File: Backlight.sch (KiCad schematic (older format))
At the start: 29 parts, among them Q201 FDN5618P, Q202 FDN5618P, U201 TPS61181, U202 TPS61181

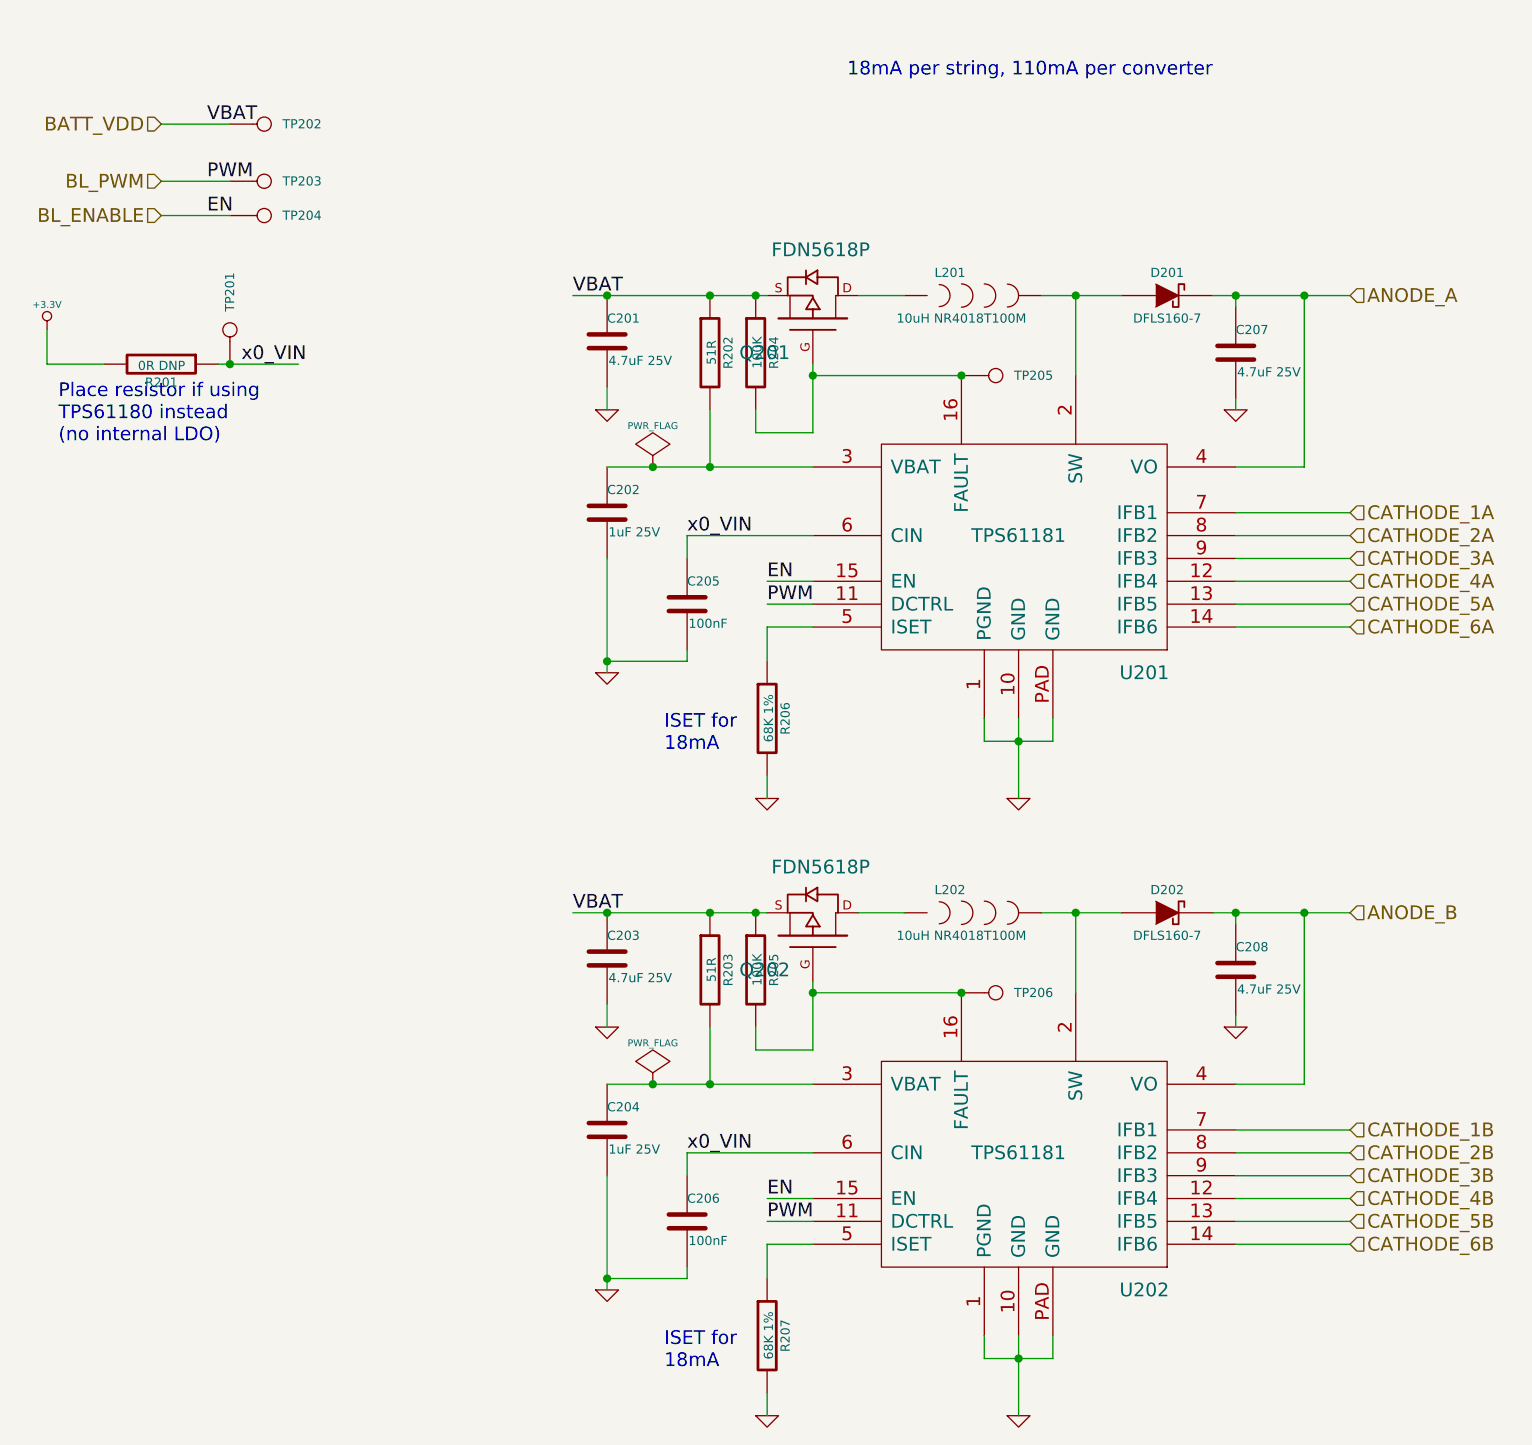
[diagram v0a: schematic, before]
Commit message: Swap fault/slow start FET for inrush current limiting thermistor
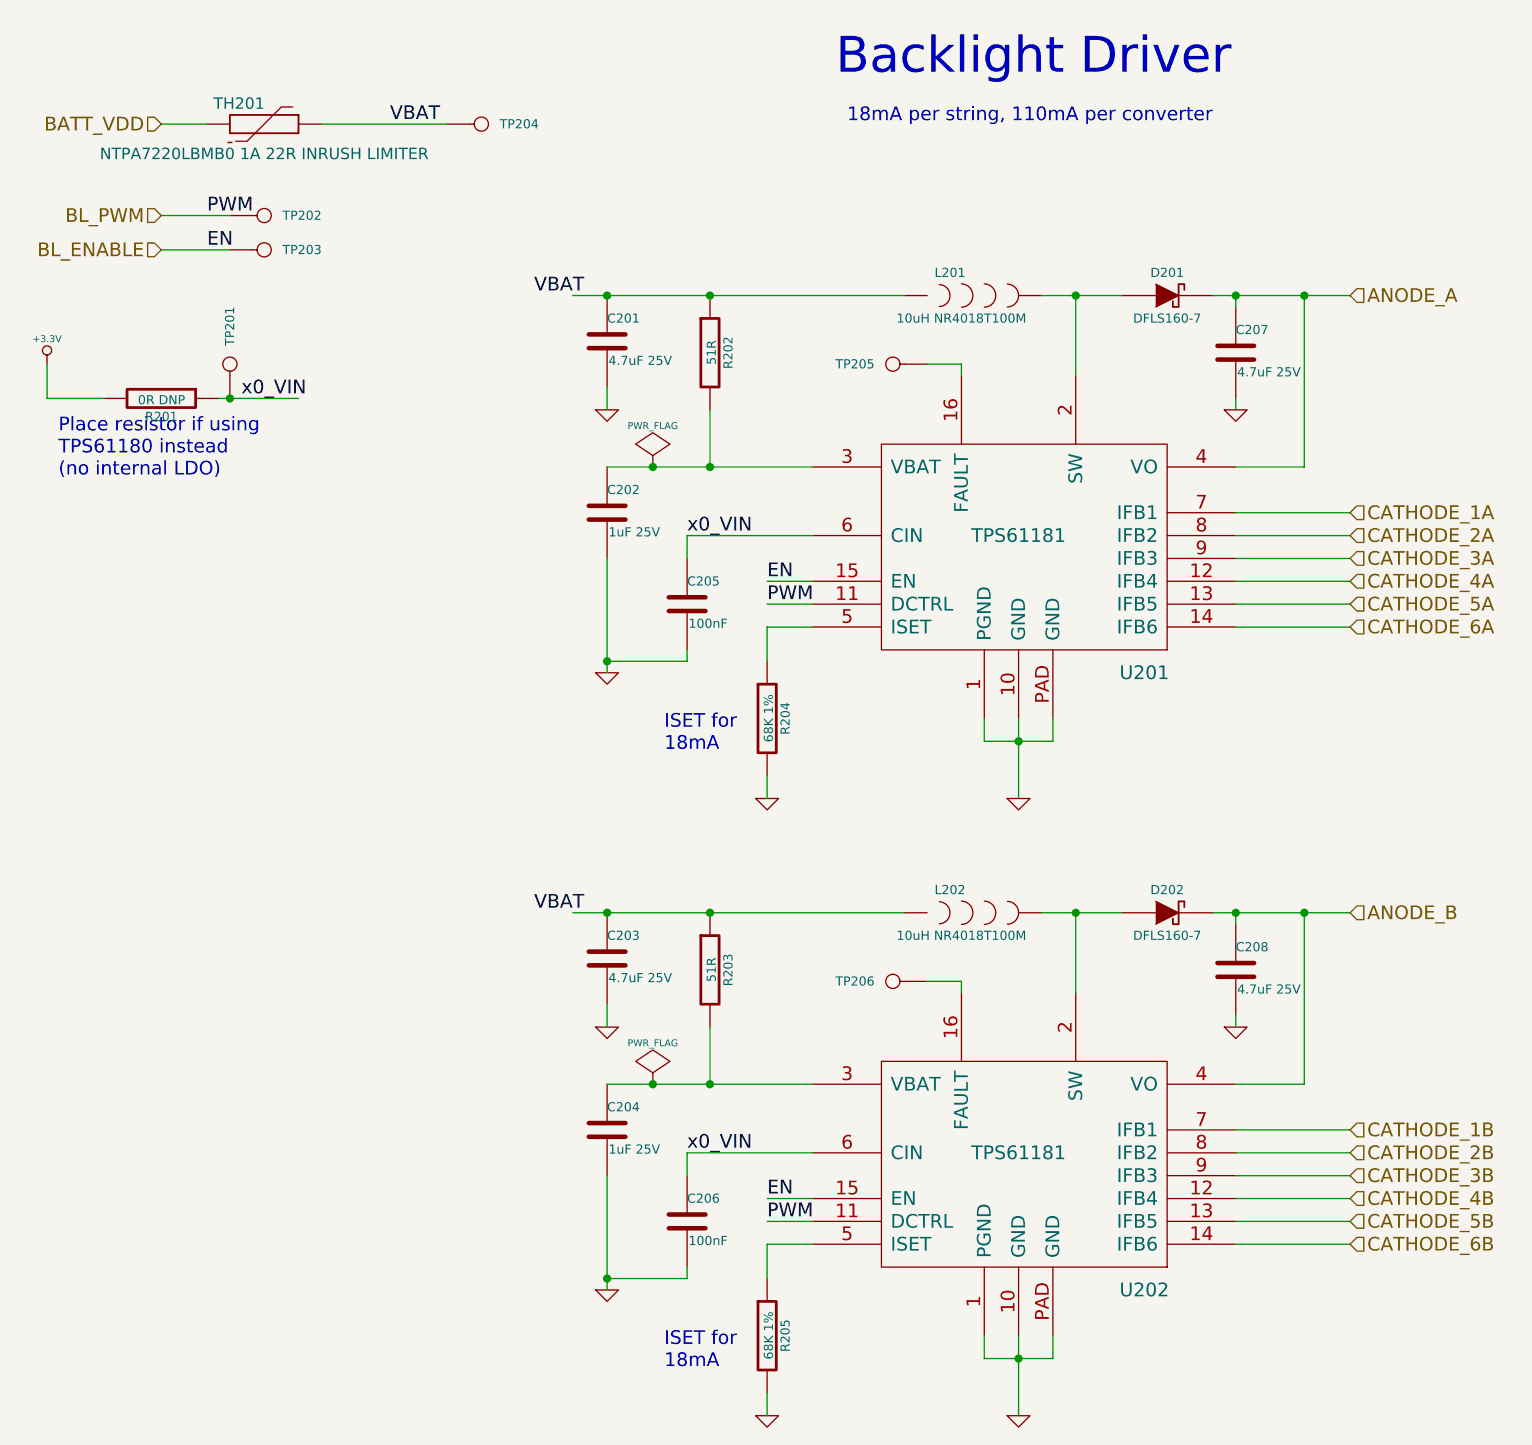
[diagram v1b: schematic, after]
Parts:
- removed Q201, Q202: FDN5618P, symbol MOSFET_P
- removed R204, R205: 100K, symbol R
- added TH201: NTPA7220LBMB0 1A 22R INRUSH LIMITER, symbol THERMISTOR
- renumbered R206 to R204, R207 to R205, TP203 to TP202, TP204 to TP203, TP202 to TP204
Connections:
- wire segments 78 -> 73
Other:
- note added: "Backlight Driver"
- moved on the sheet: R201, TP201, TP202, TP203, TP204, TP205, TP206
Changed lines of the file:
@@
 Text HLabel 6550 5900 2    60   Input ~ 0
 CATHODE_6B
+Text HLabel 1350 1550 0    60   Input ~ 0
+BL_ENABLE
 Text HLabel 1350 1400 0    60   Input ~ 0
-BL_ENABLE
-Text HLabel 1350 1250 0    60   Input ~ 0
 BL_PWM
 Text HLabel 1350 1000 0    60   Input ~ 0
 BATT_VDD
-Text Label 1700 2050 0    60   ~ 0
+Text Label 1700 2200 0    60   ~ 0
 x0_VIN
 Wire Wire Line
-	1600 2050 1950 2050
-Wire Wire Line
-	1100 2050 850  2050
-Wire Wire Line
-	850  2050 850  1900
+	1600 2200 1950 2200
+Wire Wire Line
+	1100 2200 850  2200
+Wire Wire Line
+	850  2200 850  2050
 $Comp
 L R R201
 U 1 1 54489345
-P 1350 2050
-F 0 "R201" V 1430 2050 40  0000 C CNN
-F 1 "0R DNP" V 1357 2051 40  0000 C CNN
-F 2 "" V 1280 2050 30  0000 C CNN
-F 3 "" H 1350 2050 30  0000 C CNN
-	1    1350 2050
+P 1350 2200
+F 0 "R201" V 1430 2200 40  0000 C CNN
+F 1 "0R DNP" V 1357 2201 40  0000 C CNN
+F 2 "" V 1280 2200 30  0000 C CNN
+F 3 "" H 1350 2200 30  0000 C CNN
+	1    1350 2200
 	0    1    1    0
 $EndComp
@@
 L +3.3V #PWR07
 U 1 1 544893BF
-P 850 1900
-F 0 "#PWR07" H 850 1860 30  0001 C CNN
-F 1 "+3.3V" H 850 2010 30  0000 C CNN
-F 2 "" H 850 1900 60  0000 C CNN
-F 3 "" H 850 1900 60  0000 C CNN
-	1    850  1900
-	1    0    0    -1
-$EndComp
-Text Notes 900  2400 0    60   ~ 0
+P 850 2050
+F 0 "#PWR07" H 850 2010 30  0001 C CNN
+F 1 "+3.3V" H 850 2160 30  0000 C CNN
+F 2 "" H 850 2050 60  0000 C CNN
+F 3 "" H 850 2050 60  0000 C CNN
+	1    850  2050
+	1    0    0    -1
+$EndComp
+Text Notes 900  2550 0    60   ~ 0
 Place resistor if using\nTPS61180 instead\n(no internal LDO)
 Wire Wire Line
-	1350 1250 1650 1250
-Wire Wire Line
 	1350 1400 1650 1400
+Wire Wire Line
+	1350 1550 1650 1550
+Text Label 1550 1550 0    60   ~ 0
+EN
 Text Label 1550 1400 0    60   ~ 0
-EN
-Text Label 1550 1250 0    60   ~ 0
 PWM
 $Comp
-L CONN_1 TP203
+L CONN_1 TP202
 U 1 1 54489845
-P 1800 1250
-F 0 "TP203" H 1880 1250 40  0000 L CNN
-F 1 "CONN_1" H 1800 1305 30  0001 C CNN
-F 2 "" H 1800 1250 60  0000 C CNN
-F 3 "" H 1800 1250 60  0000 C CNN
-	1    1800 1250
-	1    0    0    -1
-$EndComp
-$Comp
-L CONN_1 TP204
-U 1 1 544898A9
 P 1800 1400
-F 0 "TP204" H 1880 1400 40  0000 L CNN
+F 0 "TP202" H 1880 1400 40  0000 L CNN
 F 1 "CONN_1" H 1800 1455 30  0001 C CNN
 F 2 "" H 1800 1400 60  0000 C CNN
@@
 $EndComp
 $Comp
+L CONN_1 TP203
+U 1 1 544898A9
+P 1800 1550
+F 0 "TP203" H 1880 1550 40  0000 L CNN
+F 1 "CONN_1" H 1800 1605 30  0001 C CNN
+F 2 "" H 1800 1550 60  0000 C CNN
+F 3 "" H 1800 1550 60  0000 C CNN
+	1    1800 1550
+	1    0    0    -1
+$EndComp
+$Comp
 L CONN_1 TP201
 U 1 1 544898C7
-P 1650 1900
-F 0 "TP201" H 1730 1900 40  0000 L CNN
-F 1 "CONN_1" H 1650 1955 30  0001 C CNN
-F 2 "" H 1650 1900 60  0000 C CNN
-F 3 "" H 1650 1900 60  0000 C CNN
-	1    1650 1900
+P 1650 2050
+F 0 "TP201" H 1730 2050 40  0000 L CNN
+F 1 "CONN_1" H 1650 2105 30  0001 C CNN
+F 2 "" H 1650 2050 60  0000 C CNN
+F 3 "" H 1650 2050 60  0000 C CNN
+	1    1650 2050
 	0    -1   -1   0
 $EndComp
-Connection ~ 1650 2050
-Text Label 1550 1000 0    60   ~ 0
+Connection ~ 1650 2200
+Text Label 2350 1000 0    60   ~ 0
 VBAT
 $Comp
-L CONN_1 TP202
+L CONN_1 TP204
 U 1 1 5448A919
-P 1800 1000
-F 0 "TP202" H 1880 1000 40  0000 L CNN
-F 1 "CONN_1" H 1800 1055 30  0001 C CNN
-F 2 "" H 1800 1000 60  0000 C CNN
-F 3 "" H 1800 1000 60  0000 C CNN
-	1    1800 1000
-	1    0    0    -1
-$EndComp
-Wire Wire Line
-	1350 1000 1650 1000
-Text Notes 4350 800  0    60   ~ 0
+P 2750 1000
+F 0 "TP204" H 2830 1000 40  0000 L CNN
+F 1 "CONN_1" H 2750 1055 30  0001 C CNN
+F 2 "" H 2750 1000 60  0000 C CNN
+F 3 "" H 2750 1000 60  0000 C CNN
+	1    2750 1000
+	1    0    0    -1
+$EndComp
+Wire Wire Line
+	2050 1000 2600 1000
+Text Notes 4350 1000 0    60   ~ 0
 18mA per string, 110mA per converter\n
 $Comp
@@
 	4000 5900 4000 6050
 $Comp
-L R R207
+L R R205
 U 1 1 544804B0
 P 4000 6300
-F 0 "R207" V 4080 6300 40  0000 C CNN
+F 0 "R205" V 4080 6300 40  0000 C CNN
 F 1 "68K 1%" V 4007 6301 40  0000 C CNN
 F 2 "" V 3930 6300 30  0000 C CNN
@@
 	1    0    0    -1
 $EndComp
-Text Label 3150 4450 0    60   ~ 0
+Text Label 3200 4450 2    60   ~ 0
 VBAT
 $Comp
@@
 L CONN_1 TP206
 U 1 1 544804CF
-P 5000 4800
-F 0 "TP206" H 5080 4800 40  0000 L CNN
-F 1 "CONN_1" H 5000 4855 30  0001 C CNN
-F 2 "" H 5000 4800 60  0000 C CNN
-F 3 "" H 5000 4800 60  0000 C CNN
-	1    5000 4800
-	1    0    0    -1
-$EndComp
-Wire Wire Line
-	4200 4800 4850 4800
+P 4550 4750
+F 0 "TP206" H 4630 4750 40  0000 L CNN
+F 1 "CONN_1" H 4550 4805 30  0001 C CNN
+F 2 "" H 4550 4750 60  0000 C CNN
+F 3 "" H 4550 4750 60  0000 C CNN
+	1    4550 4750
+	-1   0    0    1
+$EndComp
 Wire Wire Line
 	5200 4450 5550 4450
@@
 Text Notes 3550 6450 0    60   ~ 0
 ISET for\n18mA
-$Comp
-L MOSFET_P Q202
-U 1 1 544804F9
-P 4200 4550
-F 0 "Q202" V 4050 4450 60  0000 R CNN
-F 1 "FDN5618P" V 4500 4800 60  0000 R CNN
-F 2 "" H 4200 4550 60  0000 C CNN
-F 3 "" H 4200 4550 60  0000 C CNN
-	1    4200 4550
-	0    1    -1   0
-$EndComp
-Connection ~ 4850 4800
-Wire Wire Line
-	4200 4750 4200 5050
-$Comp
-L R R205
-U 1 1 54480501
-P 3950 4700
-F 0 "R205" V 4030 4700 40  0000 C CNN
-F 1 "100K" V 3957 4701 40  0000 C CNN
-F 2 "" V 3880 4700 30  0000 C CNN
-F 3 "" H 3950 4700 30  0000 C CNN
-	1    3950 4700
-	1    0    0    -1
-$EndComp
-Wire Wire Line
-	3950 4950 3950 5050
-Wire Wire Line
-	3950 5050 4200 5050
-Connection ~ 4200 4800
-Wire Wire Line
-	3150 4450 4000 4450
-Connection ~ 3950 4450
-Wire Wire Line
-	4400 4450 4600 4450
+Wire Wire Line
+	3150 4450 4600 4450
 Wire Wire Line
 	3650 5600 3650 5500
@@
 	4000 3200 4000 3350
 $Comp
-L R R206
+L R R204
 U 1 1 544897C1
 P 4000 3600
-F 0 "R206" V 4080 3600 40  0000 C CNN
+F 0 "R204" V 4080 3600 40  0000 C CNN
 F 1 "68K 1%" V 4007 3601 40  0000 C CNN
 F 2 "" V 3930 3600 30  0000 C CNN
@@
 	1    0    0    -1
 $EndComp
-Text Label 3150 1750 0    60   ~ 0
+Text Label 3200 1750 2    60   ~ 0
 VBAT
 $Comp
@@
 L CONN_1 TP205
 U 1 1 544897E0
-P 5000 2100
-F 0 "TP205" H 5080 2100 40  0000 L CNN
-F 1 "CONN_1" H 5000 2155 30  0001 C CNN
-F 2 "" H 5000 2100 60  0000 C CNN
-F 3 "" H 5000 2100 60  0000 C CNN
-	1    5000 2100
-	1    0    0    -1
-$EndComp
-Wire Wire Line
-	4200 2100 4850 2100
+P 4550 2050
+F 0 "TP205" H 4630 2050 40  0000 L CNN
+F 1 "CONN_1" H 4550 2105 30  0001 C CNN
+F 2 "" H 4550 2050 60  0000 C CNN
+F 3 "" H 4550 2050 60  0000 C CNN
+	1    4550 2050
+	-1   0    0    1
+$EndComp
 Wire Wire Line
 	5200 1750 5550 1750
@@
 Text Notes 3550 3750 0    60   ~ 0
 ISET for\n18mA
-$Comp
-L MOSFET_P Q201
-U 1 1 5448980A
-P 4200 1850
-F 0 "Q201" V 4050 1750 60  0000 R CNN
-F 1 "FDN5618P" V 4500 2100 60  0000 R CNN
-F 2 "" H 4200 1850 60  0000 C CNN
-F 3 "" H 4200 1850 60  0000 C CNN
-	1    4200 1850
-	0    1    -1   0
-$EndComp
-Connection ~ 4850 2100
-Wire Wire Line
-	4200 2050 4200 2350
-$Comp
-L R R204
-U 1 1 54489812
-P 3950 2000
-F 0 "R204" V 4030 2000 40  0000 C CNN
-F 1 "100K" V 3957 2001 40  0000 C CNN
-F 2 "" V 3880 2000 30  0000 C CNN
-F 3 "" H 3950 2000 30  0000 C CNN
-	1    3950 2000
-	1    0    0    -1
-$EndComp
-Wire Wire Line
-	3950 2250 3950 2350
-Wire Wire Line
-	3950 2350 4200 2350
-Connection ~ 4200 2100
-Wire Wire Line
-	3150 1750 4000 1750
-Connection ~ 3950 1750
-Wire Wire Line
-	4400 1750 4600 1750
+Wire Wire Line
+	3150 1750 4600 1750
 Wire Wire Line
 	3650 2900 3650 2800
@@
 	1    0    0    -1
 $EndComp
+Text Notes 4300 800  0    157  ~ 0
+Backlight Driver
+Wire Wire Line
+	4700 2050 4850 2050
+Wire Wire Line
+	4850 2050 4850 2100
+Wire Wire Line
+	4850 4800 4850 4750
+Wire Wire Line
+	4850 4750 4700 4750
+$Comp
+L THERMISTOR TH201
+U 1 1 54591CF8
+P 1800 1000
+F 0 "TH201" V 1710 890 50  0000 C CNN
+F 1 "NTPA7220LBMB0 1A 22R INRUSH LIMITER" V 1930 1000 50  0000 C CNN
+F 2 "" H 1800 1000 60  0000 C CNN
+F 3 "" H 1800 1000 60  0000 C CNN
+	1    1800 1000
+	0    1    1    0
+$EndComp
+Wire Wire Line
+	1550 1000 1350 1000
 $EndSCHEMATC
